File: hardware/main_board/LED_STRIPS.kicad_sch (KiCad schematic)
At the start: 2 parts, among them J12 373, J13 Conn_01x03_Pin

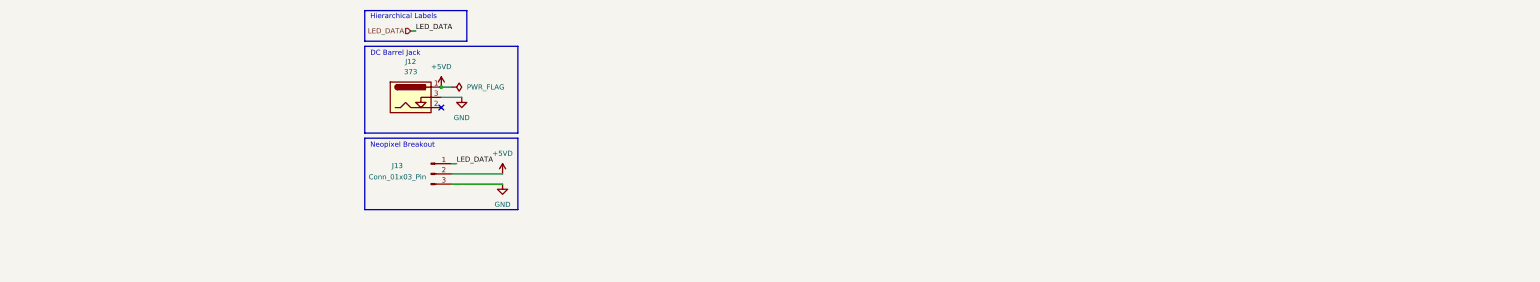
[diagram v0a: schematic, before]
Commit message: main board stuff. removed usbc for power. added level shifter for led logic signal. added lights for mux select signals. finished layout + pass DRC
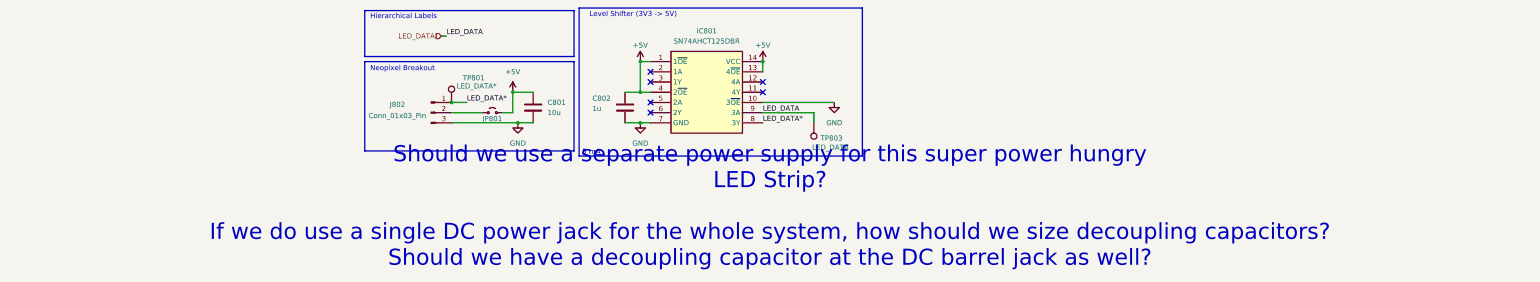
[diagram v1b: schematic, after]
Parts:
- removed J12: 373, 373, symbol SamacSys_Parts:Barrel_Jack
- added C801: 10u, Capacitor_SMD:C_0805_2012Metric, symbol ECE445L:C
- added C802: 1u, Capacitor_SMD:C_0805_2012Metric, symbol ECE445L:C
- added IC801: SN74AHCT125DBR, SamacSys_Parts:SOP65P780X200-14N, symbol SamacSys_Parts:SN74AHCT125DBR
- added JP801: Jumper_2_Small_Bridged, 445L:PinHeader_1x02_P2.54mm_Vertical, symbol Jumper:Jumper_2_Small_Open
- added TP801: LED_DATA*, SamacSys_Parts:bettertestpoint2, symbol Connector:TestPoint
- added TP803: LED_DATA, SamacSys_Parts:bettertestpoint2, symbol Connector:TestPoint
- renumbered J13 to J802
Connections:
- net GND: now also C801.2, C802.2, IC801.10 (3~{OE}), IC801.7 (GND)
- net LED_DATA: now also IC801.9 (3A), TP803.1; no longer J802.1 (Pin_1)
- net +5VD: no longer names the net of J802.2 (Pin_2)
- net +5VD: now also JP801.1 (A)
- new net +5V: C801.1, C802.1, IC801.1 (1~{OE}), IC801.13 (4~{OE}), IC801.14 (VCC), IC801.4 (2~{OE}), JP801.2 (B)
- new net LED_DATA*: IC801.8 (3Y), J802.1 (Pin_1), TP801.1
- no-connect marks 1 -> 6
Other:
- note added: "5 mA"
- note added: "Level Shifter (3V3 -> 5V)"
- note added: "Should we use a separate power supply for this super power hungry LED Strip? If we do use a single DC power jack for the whole system, how should we size decoupling capacitors? Should we have a decoupling capacitor at the DC barrel jack as well?"
- note removed: "DC Barrel Jack"
- moved on the sheet: J802

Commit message: bom
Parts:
- added J801: Conn_01x03_Pin, Connector_PinHeader_2.54mm:PinHeader_1x03_P2.54mm_Vertical, symbol Connector:Conn_01x03_Pin
- added U801: ~, symbol SamacSys_Parts:led_strip
- J802, JP801: now left out of the parts list
- TP801: value LED_DATA* -> LED_D
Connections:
- net LED_DATA: now also J801.1 (Pin_1)
- net LED_DATA*: now also J801.3 (Pin_3); no longer J802.1 (Pin_1), TP801.1
- new net LED_D: J801.2 (Pin_2), J802.1 (Pin_1), TP801.1
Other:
- note added: "2A max"
- note added: "Choose between 3V3 Logic Level and 5V Logic"
- note added: "Neopixel Strip"
- note removed: "Should we use a separate power supply for this super power hungry LED Strip? If we do use a single DC power jack for the whole system, how should we size decoupling capacitors? Should we have a decoupling capacitor at the DC barrel jack as well?"
- moved on the sheet: C801, C802, IC801, J802, JP801, TP801, TP803
